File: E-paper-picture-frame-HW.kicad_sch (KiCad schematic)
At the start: 8 parts

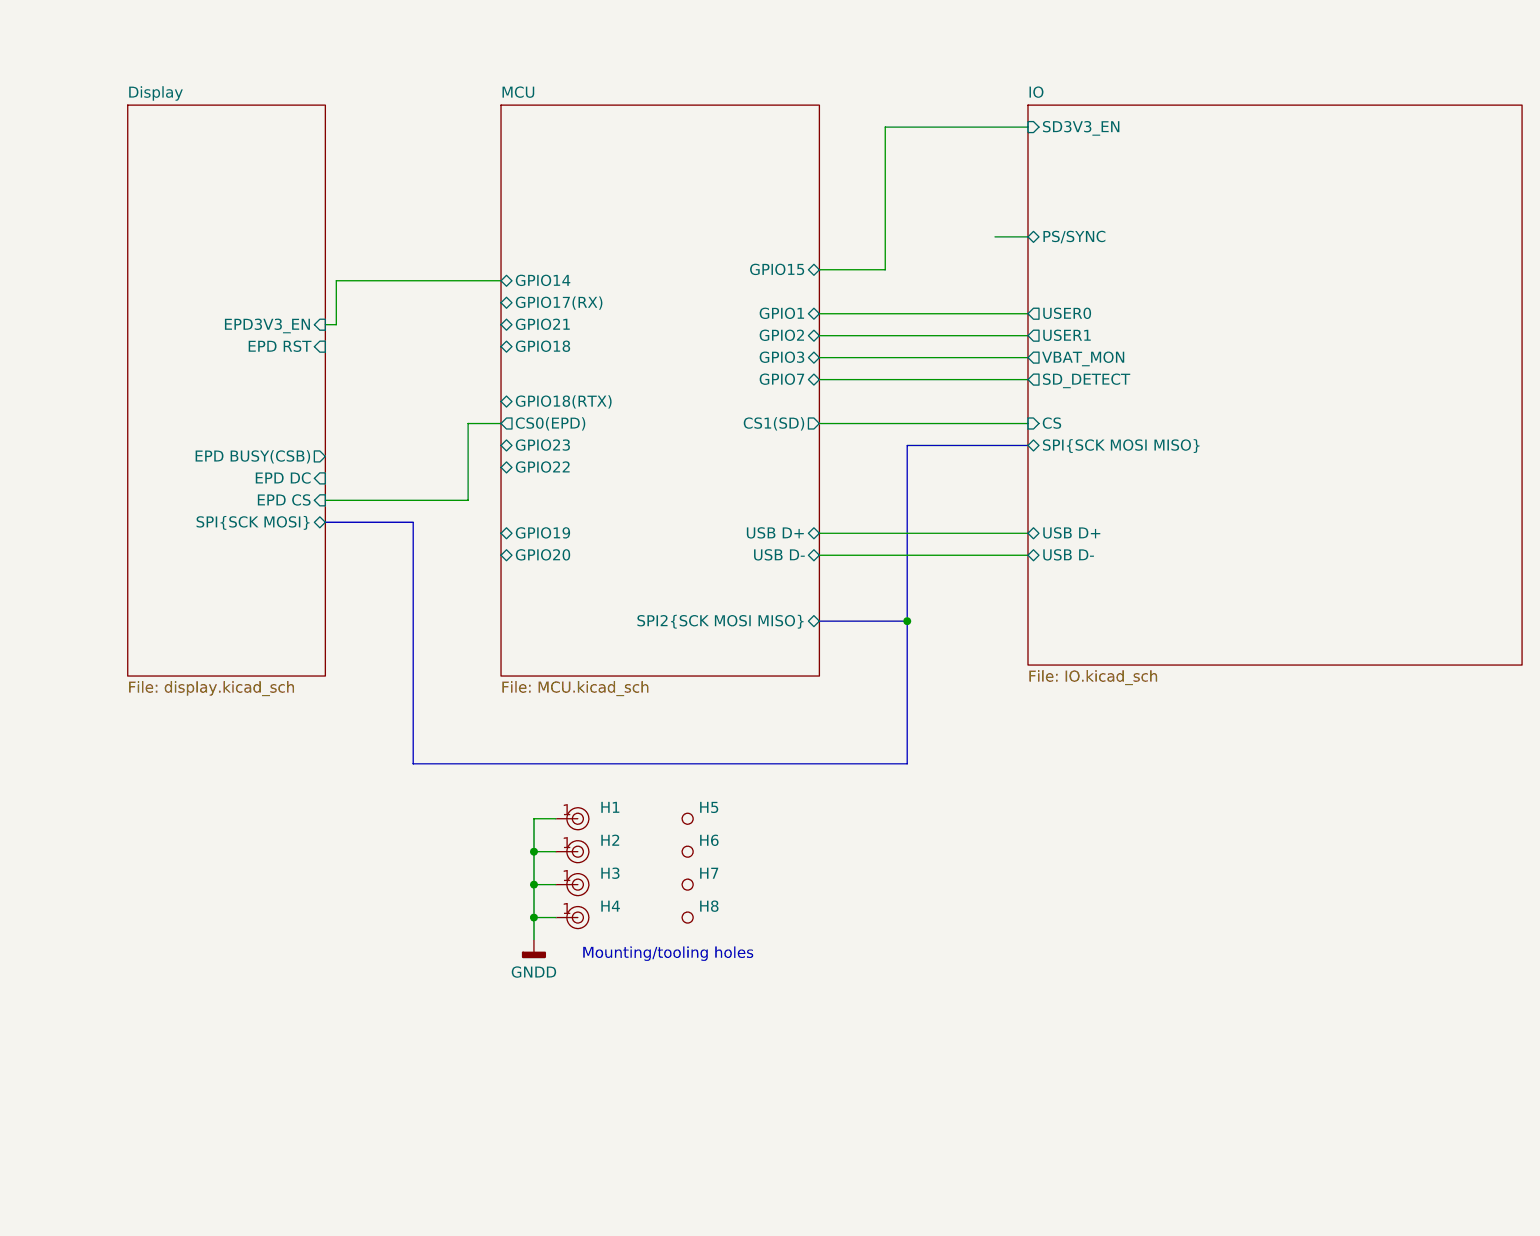
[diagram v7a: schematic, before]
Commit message: Changed some parts for more common ones
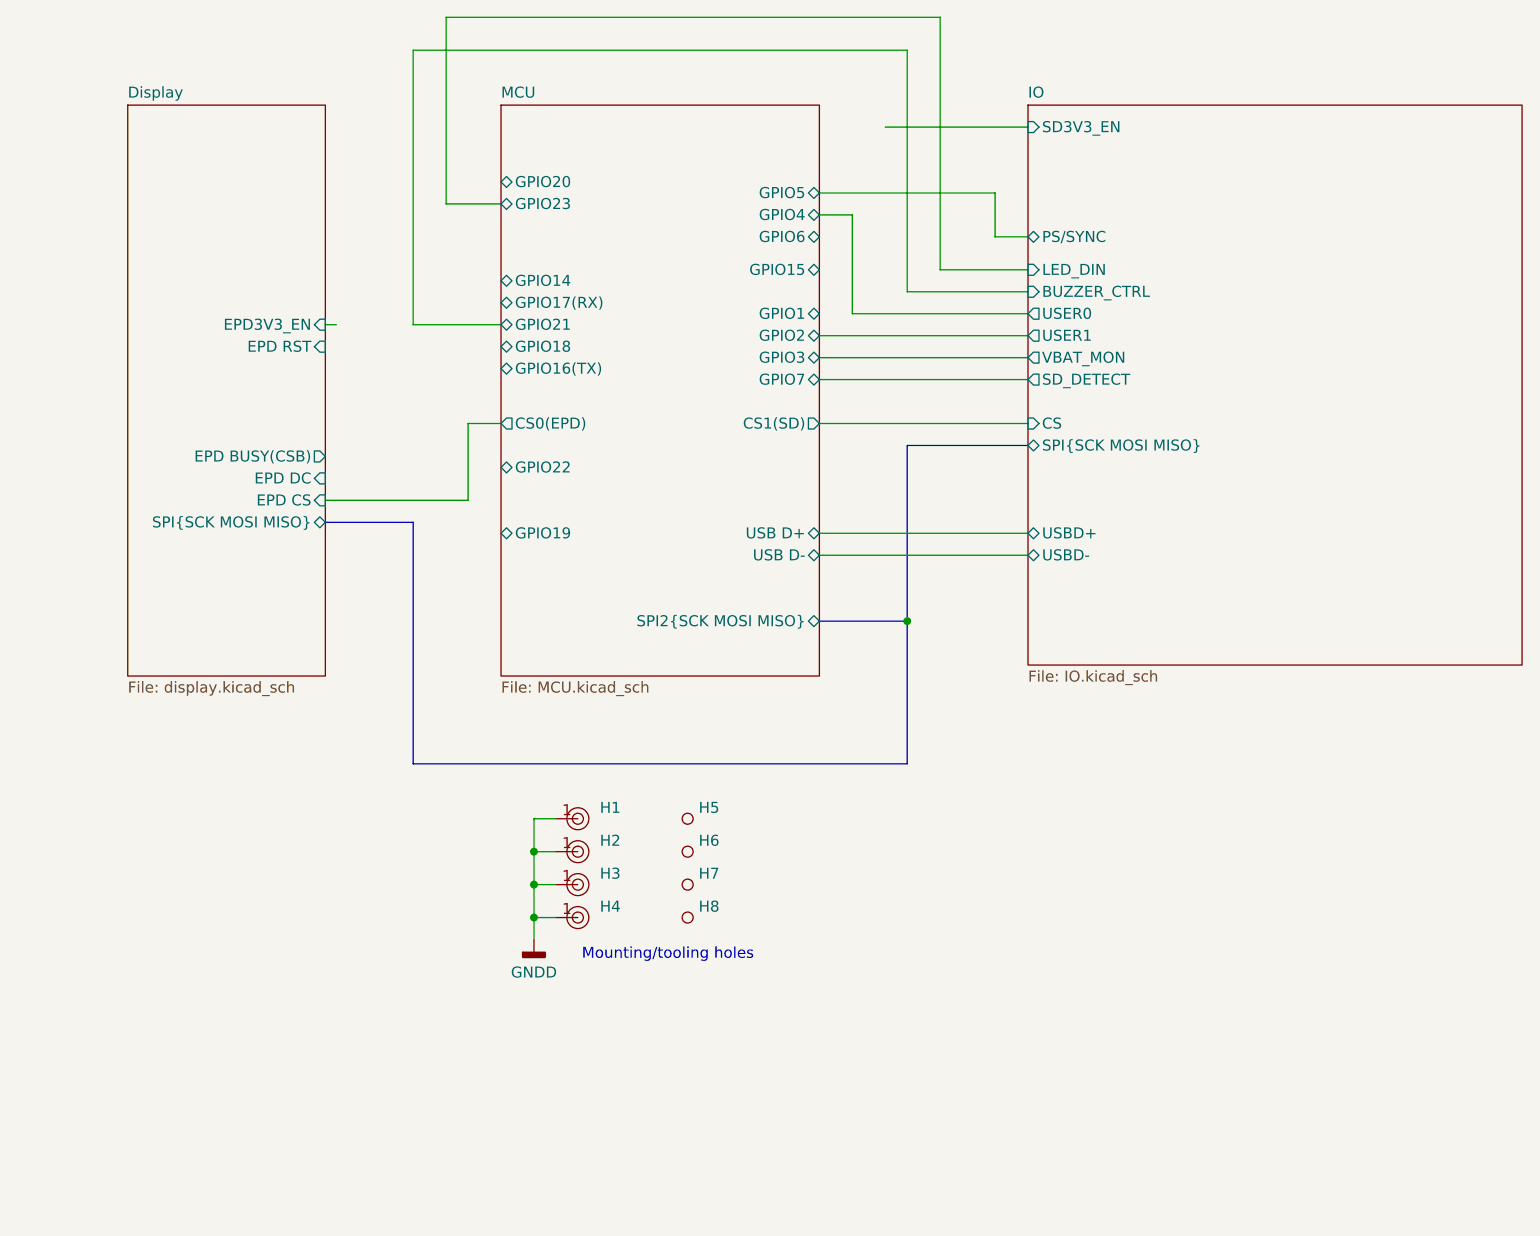
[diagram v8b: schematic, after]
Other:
- sheet Display ports: added SPI{SCK MOSI MISO}; removed SPI{SCK MOSI}
- sheet IO ports: added BUZZER_CTRL, LED_DIN, USBD+, USBD-; removed USB D+, USB D-
- sheet MCU ports: added GPIO16(TX), GPIO4, GPIO5, GPIO6; removed GPIO18(RTX)
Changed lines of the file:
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@@
 		(color 0 0 0 0)
 	)
-	(wire
-		(pts
-			(xy 151.13 63.5) (xy 158.75 63.5)
-		)
-		(stroke
-			(width 0)
-			(type default)
-		)
-	)
 	(bus
 		(pts
@@
 	(wire
 		(pts
+			(xy 154.94 57.15) (xy 154.94 68.58)
+		)
+		(stroke
+			(width 0)
+			(type default)
+		)
+	)
+	(wire
+		(pts
+			(xy 104.14 69.85) (xy 104.14 38.1)
+		)
+		(stroke
+			(width 0)
+			(type default)
+		)
+	)
+	(wire
+		(pts
 			(xy 171.45 59.69) (xy 175.26 59.69)
 		)
@@
 	(wire
 		(pts
+			(xy 165.1 63.5) (xy 175.26 63.5)
+		)
+		(stroke
+			(width 0)
+			(type default)
+		)
+	)
+	(wire
+		(pts
 			(xy 110.49 90.17) (xy 110.49 81.28)
 		)
@@
 	(wire
 		(pts
+			(xy 151.13 57.15) (xy 154.94 57.15)
+		)
+		(stroke
+			(width 0)
+			(type default)
+		)
+	)
+	(wire
+		(pts
+			(xy 161.29 66.04) (xy 161.29 38.1)
+		)
+		(stroke
+			(width 0)
+			(type default)
+		)
+	)
+	(wire
+		(pts
+			(xy 107.95 34.29) (xy 165.1 34.29)
+		)
+		(stroke
+			(width 0)
+			(type default)
+		)
+	)
+	(wire
+		(pts
 			(xy 151.13 93.98) (xy 175.26 93.98)
 		)
@@
 	(wire
 		(pts
-			(xy 95.25 69.85) (xy 95.25 64.77)
-		)
-		(stroke
-			(width 0)
-			(type default)
-		)
-	)
-	(wire
-		(pts
 			(xy 158.75 46.99) (xy 175.26 46.99)
 		)
@@
 	(wire
 		(pts
+			(xy 151.13 54.61) (xy 171.45 54.61)
+		)
+		(stroke
+			(width 0)
+			(type default)
+		)
+	)
+	(wire
+		(pts
 			(xy 118.11 130.81) (xy 120.65 130.81)
 		)
@@
 	(wire
 		(pts
-			(xy 158.75 63.5) (xy 158.75 46.99)
+			(xy 104.14 38.1) (xy 161.29 38.1)
+		)
+		(stroke
+			(width 0)
+			(type default)
+		)
+	)
+	(wire
+		(pts
+			(xy 165.1 34.29) (xy 165.1 63.5)
+		)
+		(stroke
+			(width 0)
+			(type default)
+		)
+	)
+	(wire
+		(pts
+			(xy 114.3 55.88) (xy 107.95 55.88)
 		)
 		(stroke
@@
 	(wire
 		(pts
+			(xy 107.95 55.88) (xy 107.95 34.29)
+		)
+		(stroke
+			(width 0)
+			(type default)
+		)
+	)
+	(wire
+		(pts
+			(xy 171.45 54.61) (xy 171.45 59.69)
+		)
+		(stroke
+			(width 0)
+			(type default)
+		)
+	)
+	(wire
+		(pts
 			(xy 118.11 138.43) (xy 118.11 140.97)
 		)
@@
 		)
 	)
+	(wire
+		(pts
+			(xy 175.26 66.04) (xy 161.29 66.04)
+		)
+		(stroke
+			(width 0)
+			(type default)
+		)
+	)
 	(bus
 		(pts
@@
 	(wire
 		(pts
+			(xy 154.94 68.58) (xy 175.26 68.58)
+		)
+		(stroke
+			(width 0)
+			(type default)
+		)
+	)
+	(wire
+		(pts
 			(xy 93.98 69.85) (xy 95.25 69.85)
 		)
@@
 		)
 	)
-	(wire
-		(pts
-			(xy 95.25 64.77) (xy 114.3 64.77)
-		)
-		(stroke
-			(width 0)
-			(type default)
-		)
-	)
 	(bus
 		(pts
@@
 	(wire
 		(pts
-			(xy 151.13 68.58) (xy 175.26 68.58)
-		)
-		(stroke
-			(width 0)
-			(type default)
-		)
-	)
-	(wire
-		(pts
 			(xy 93.98 90.17) (xy 110.49 90.17)
 		)
@@
 		(pts
 			(xy 118.11 127) (xy 118.11 130.81)
+		)
+		(stroke
+			(width 0)
+			(type default)
+		)
+	)
+	(wire
+		(pts
+			(xy 114.3 69.85) (xy 104.14 69.85)
 		)
 		(stroke
@@
 		(dnp no)
 		(fields_autoplaced yes)
-		(property "Reference" "#PWR051"
+		(property "Reference" "#PWR01"
 			(at 118.11 147.32 0)
 			(effects
@@
 			(project ""
 				(path "/84f37c25-92ec-4cd3-b0ad-d93e10e73cdb"
-					(reference "#PWR051")
+					(reference "#PWR01")
 					(unit 1)
 				)
@@
 			)
 		)
-		(pin "SPI{SCK MOSI}" bidirectional
+		(pin "SPI{SCK MOSI MISO}" bidirectional
 			(at 93.98 92.71 0)
 			(effects
@@
 			)
 		)
-		(pin "GPIO18(RTX)" bidirectional
-			(at 114.3 78.74 180)
-			(effects
-				(font
-					(size 1.27 1.27)
-				)
-				(justify left)
-			)
-		)
 		(pin "GPIO14" bidirectional
 			(at 114.3 64.77 180)
@@
 		)
 		(pin "GPIO23" bidirectional
-			(at 114.3 83.82 180)
+			(at 114.3 55.88 180)
 			(effects
 				(font
@@
 		)
 		(pin "GPIO20" bidirectional
-			(at 114.3 96.52 180)
+			(at 114.3 53.34 180)
 			(effects
 				(font
@@
 		(pin "GPIO1" bidirectional
 			(at 151.13 68.58 0)
+			(effects
+				(font
+					(size 1.27 1.27)
+				)
+				(justify right)
+			)
+		)
+		(pin "GPIO16(TX)" bidirectional
+			(at 114.3 74.93 180)
+			(effects
+				(font
+					(size 1.27 1.27)
+				)
+				(justify left)
+			)
+		)
+		(pin "GPIO5" bidirectional
+			(at 151.13 54.61 0)
+			(effects
+				(font
+					(size 1.27 1.27)
+				)
+				(justify right)
+			)
+		)
+		(pin "GPIO4" bidirectional
+			(at 151.13 57.15 0)
+			(effects
+				(font
+					(size 1.27 1.27)
+				)
+				(justify right)
+			)
+		)
+		(pin "GPIO6" bidirectional
+			(at 151.13 59.69 0)
 			(effects
 				(font
@@
 			)
 		)
-		(pin "USB D-" bidirectional
-			(at 175.26 96.52 180)
-			(effects
-				(font
-					(size 1.27 1.27)
-				)
-				(justify left)
-			)
-		)
-		(pin "USB D+" bidirectional
-			(at 175.26 93.98 180)
-			(effects
-				(font
-					(size 1.27 1.27)
-				)
-				(justify left)
-			)
-		)
 		(pin "SPI{SCK MOSI MISO}" bidirectional
 			(at 175.26 83.82 180)
@@
 			(effects
 				(font
+					(size 1.27 1.27)
+				)
+				(justify left)
+			)
+		)
+		(pin "LED_DIN" input
+			(at 175.26 63.5 180)
+			(effects
+				(font
+					(size 1.27 1.27)
+				)
+				(justify left)
+			)
+		)
+		(pin "BUZZER_CTRL" input
+			(at 175.26 66.04 180)
+			(effects
+				(font
+					(size 1.27 1.27)
+				)
+				(justify left)
+			)
+		)
+		(pin "USBD+" bidirectional
+			(at 175.26 93.98 180)
+			(effects
+				(font
+					(size 1.27 1.27)
+				)
+				(justify left)
+			)
+		)
+		(pin "USBD-" bidirectional
+			(at 175.26 96.52 180)
+			(effects
+				(font
